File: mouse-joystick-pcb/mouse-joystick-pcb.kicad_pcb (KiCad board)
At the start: 4 copper layers, 60 x 120 mm, 90 parts, among them J301 2.1, J501 Conn_01x02_P3.5mm_TBH_Horizon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, J502 Conn_01x04_P3.5mm_TBH_Horizon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, J503 Molex_PicoBlade_Horizontal, J701 Conn_01x02_P3.5mm_TBH_Horizon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, J702 Conn_01x04_P3.5mm_TBH_Horizon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, J801 Conn_01x02_P3.5mm_TBH_Horizon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, J901 Conn_01x04_P3.5mm_TBH_Horizon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, U301 TPSM365R6V5RDNR, U501 MAX6816, U502 TMC5130A-TA, U503 Logic_LevelTranslator_LSF0102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, U601 TPA6204A1DRBR, U701 MAX6816, U702 TMC5130A-TA, U801 40V_200mA, U901 PGA305ARHHR, X501 16MHz_3.3V, X701 16MHz_3.3V

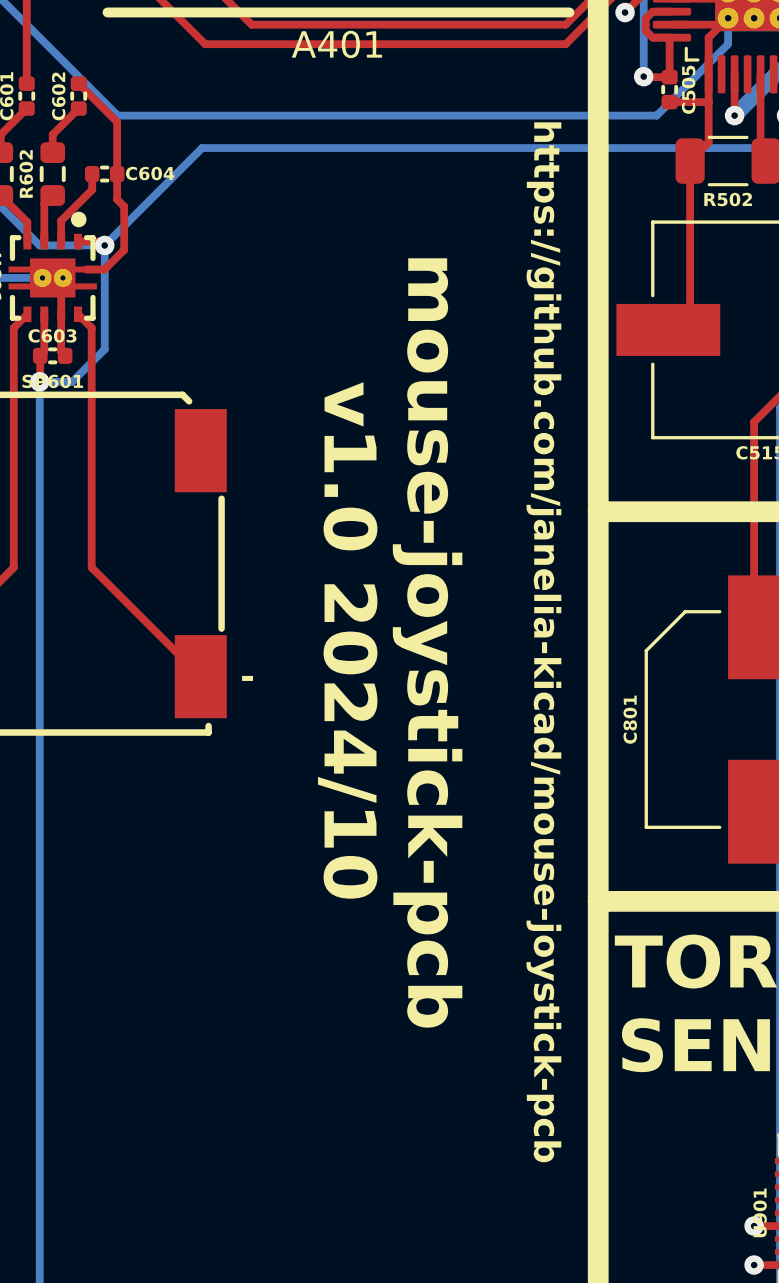
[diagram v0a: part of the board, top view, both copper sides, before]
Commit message: Update documentation for future v1.1
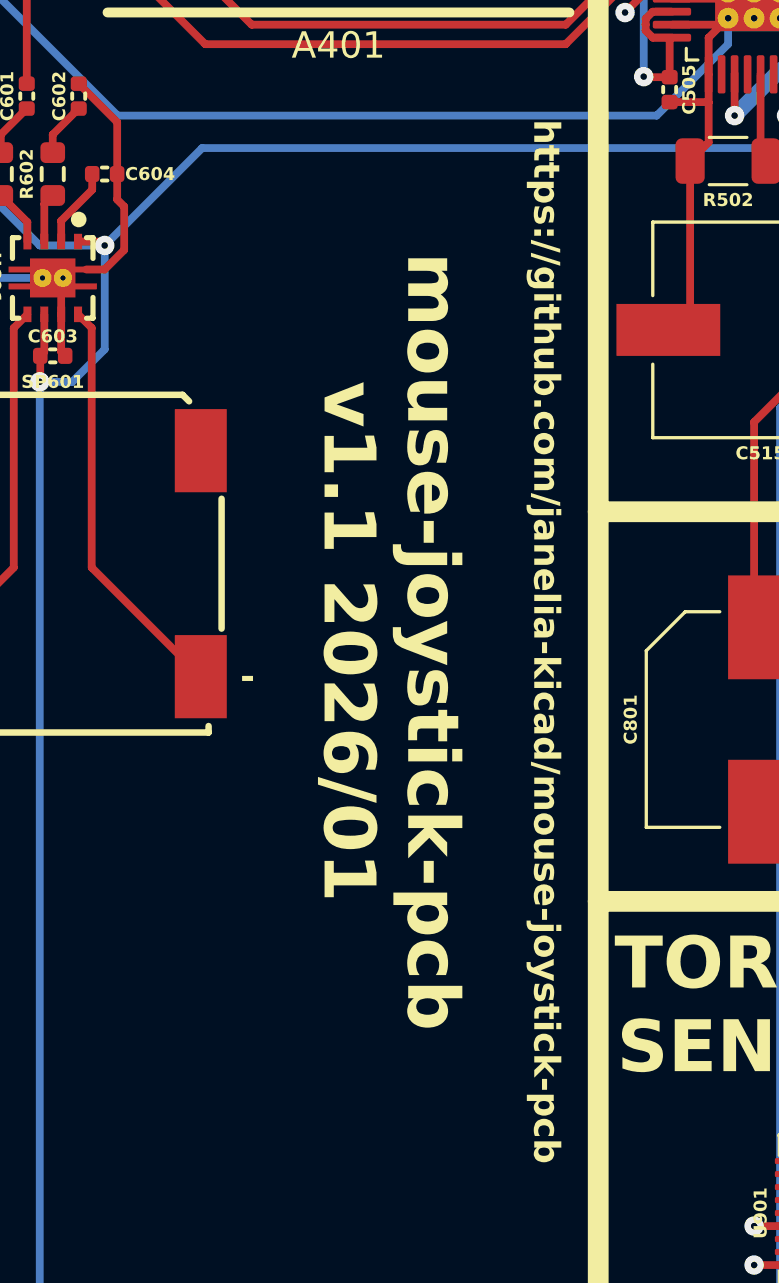
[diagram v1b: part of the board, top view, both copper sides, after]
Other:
- board text added: "mouse-joystick-pcb v1.1 2026/01"
- board text removed: "mouse-joystick-pcb v1.0 2024/10"
